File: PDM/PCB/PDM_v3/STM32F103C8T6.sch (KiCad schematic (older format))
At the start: 18 parts, among them J14 SWD, SW1 SW_SPDT, U4 STM32F103C8Tx, Y1 8MHz

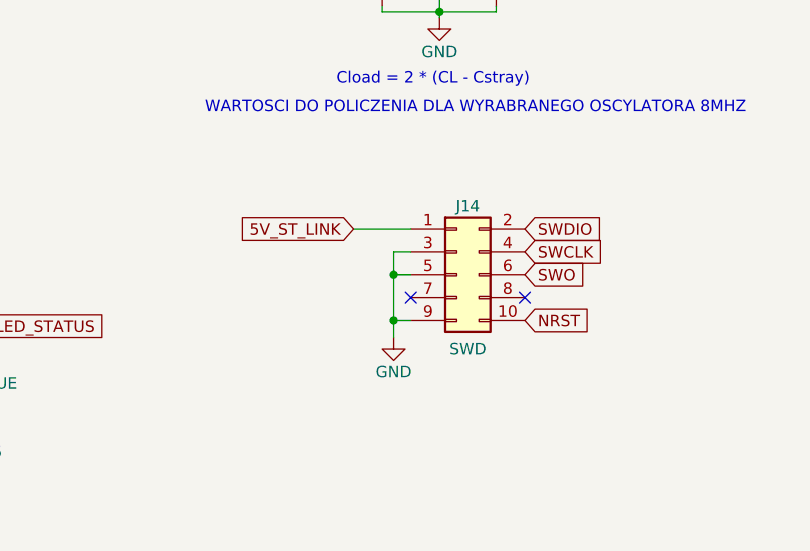
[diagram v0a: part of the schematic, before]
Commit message: Add PCB for PDM
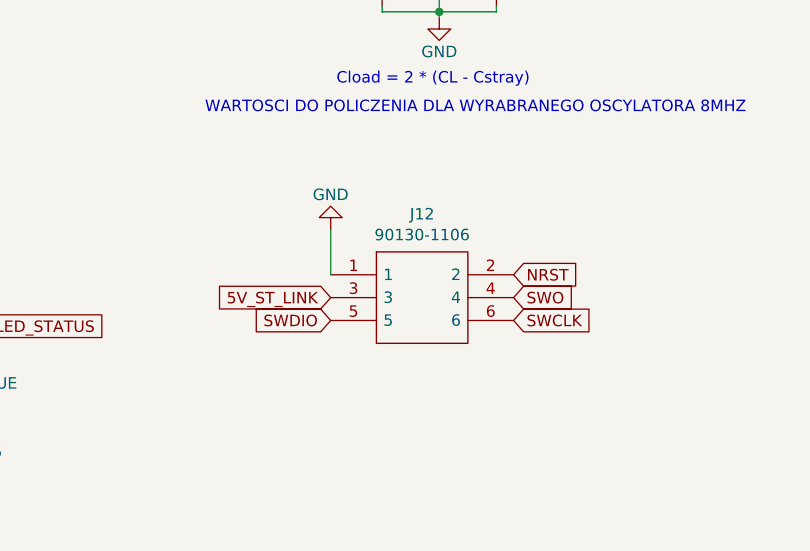
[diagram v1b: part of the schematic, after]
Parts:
- removed J14: SWD, Connector_PinHeader_1.27mm:PinHeader_2x05_P1.27mm_Vertical_SMD, symbol Connector_Generic:Conn_02x05_Odd_Even
- added J12: 90130-1106, SHDR6W65P254_2X3_996X975X1110P, symbol 90130-1106:90130-1106
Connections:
- net 5V_ST_LINK: now also J12.3
- net GND: now also J12.1
- net NRST: now also J12.2
- net SWCLK: now also J12.6
- net SWDIO: now also J12.5
- net SWO: now also J12.4
- no-connect marks 13 -> 11
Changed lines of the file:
@@
 Text Notes 6100 4650 0    50   ~ 0
 Cload = 2 * (CL - Cstray)
-$Comp
-L Connector_Generic:Conn_02x05_Odd_Even J14
-U 1 1 61927E5C
-P 6625 5475
-F 0 "J14" H 6675 5775 50  0000 C CNN
-F 1 "SWD" H 6675 5150 50  0000 C CNN
-F 2 "Connector_PinHeader_1.27mm:PinHeader_2x05_P1.27mm_Vertical_SMD" H 6625 5475 50  0001 C CNN
-F 3 "~" H 6625 5475 50  0001 C CNN
-	1    6625 5475
-	1    0    0    -1
-$EndComp
-$Comp
-L power:GND #PWR044
-U 1 1 61927E6A
-P 6350 5750
-F 0 "#PWR044" H 6350 5500 50  0001 C CNN
-F 1 "GND" H 6350 5600 50  0000 C CNN
-F 2 "" H 6350 5750 50  0001 C CNN
-F 3 "" H 6350 5750 50  0001 C CNN
-	1    6350 5750
-	1    0    0    -1
-$EndComp
-Wire Wire Line
-	6425 5375 6350 5375
-Wire Wire Line
-	6350 5375 6350 5475
-Wire Wire Line
-	6425 5475 6350 5475
-Connection ~ 6350 5475
-Wire Wire Line
-	6350 5475 6350 5675
-Wire Wire Line
-	6425 5675 6350 5675
-Connection ~ 6350 5675
-Wire Wire Line
-	6350 5675 6350 5750
-NoConn ~ 6425 5575
-Text GLabel 6925 5275 2    50   Input ~ 0
-SWDIO
-Text GLabel 6925 5375 2    50   Input ~ 0
-SWCLK
-Text GLabel 6925 5475 2    50   Input ~ 0
-SWO
-NoConn ~ 6925 5575
-Text GLabel 6925 5675 2    50   Input ~ 0
-NRST
 Wire Wire Line
 	4450 6400 4450 6300
@@
 Wire Wire Line
 	2325 1800 2325 1900
-Wire Wire Line
-	6175 5275 6425 5275
-Text GLabel 6175 5275 0    50   Input ~ 0
-5V_ST_LINK
 Text GLabel 2550 3050 0    50   Input ~ 0
 NRST
@@
 Text HLabel 2550 5650 0    50   Input ~ 0
 PB15
+$Comp
+L 90130-1106:90130-1106 J12
+U 1 1 61F4B184
+P 6075 5475
+F 0 "J12" H 6475 5740 50  0000 C CNN
+F 1 "90130-1106" H 6475 5649 50  0000 C CNN
+F 2 "SHDR6W65P254_2X3_996X975X1110P" H 6725 5575 50  0001 L CNN
+F 3 "" H 6725 5475 50  0001 L CNN
+F 4 "Headers & Wire Housings 2.54MM CGRIDIII HDR 6P V DR SHRD TIN" H 6725 5375 50  0001 L CNN "Description"
+F 5 "11.1" H 6725 5275 50  0001 L CNN "Height"
+F 6 "Molex" H 6725 5175 50  0001 L CNN "Manufacturer_Name"
+F 7 "90130-1106" H 6725 5075 50  0001 L CNN "Manufacturer_Part_Number"
+F 8 "538-90130-1106" H 6725 4975 50  0001 L CNN "Mouser Part Number"
+F 9 "https://www.mouser.co.uk/ProductDetail/Molex/90130-1106/?qs=kEwmkoUtv7SJTmEdS0xkTg%3D%3D" H 6725 4875 50  0001 L CNN "Mouser Price/Stock"
+F 10 "" H 6725 4775 50  0001 L CNN "Arrow Part Number"
+F 11 "" H 6725 4675 50  0001 L CNN "Arrow Price/Stock"
+	1    6075 5475
+	1    0    0    -1
+$EndComp
+Text GLabel 6075 5575 0    50   Input ~ 0
+5V_ST_LINK
+$Comp
+L power:GND #PWR037
+U 1 1 61F4EF21
+P 6075 5275
+F 0 "#PWR037" H 6075 5025 50  0001 C CNN
+F 1 "GND" H 6075 5125 50  0000 C CNN
+F 2 "" H 6075 5275 50  0001 C CNN
+F 3 "" H 6075 5275 50  0001 C CNN
+	1    6075 5275
+	-1   0    0    1
+$EndComp
+Wire Wire Line
+	6075 5475 6075 5275
+Text GLabel 6075 5675 0    50   Input ~ 0
+SWDIO
+Text GLabel 6875 5475 2    50   Input ~ 0
+NRST
+Text GLabel 6875 5575 2    50   Input ~ 0
+SWO
+Text GLabel 6875 5675 2    50   Input ~ 0
+SWCLK
 $EndSCHEMATC
